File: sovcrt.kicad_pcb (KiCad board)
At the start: 2 copper layers, 51.8 x 41.2 mm, 13 parts, among them J1 Conn_01x02_Male, J2 Conn_01x02_Male, J3 Conn_01x03_Male, U1 LM2575BT-ADJ

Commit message: With @'RueNahcMohr's feedback hack.
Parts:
- added D2: 1N4148, Diode_THT:D_DO-35_SOD27_P7.62mm_Horizontal, F.Cu at (114.8, 84.3)
- added RV1: 5k, Potentiometer_THT:Potentiometer_Bourns_3266P_Horizontal, F.Cu at (119.9, 102.6)
- R1: value 1k -> 4.7k
- R2: value 50 -> 220k; footprint Resistor_THT:R_Axial_DIN0207_L6.3mm_D2.5mm_P10.16mm_Horizontal -> Resistor_THT:R_Axial_DIN0204_L3.6mm_D1.6mm_P7.62mm_Horizontal
- moved R1 7.10 mm to (110.5, 92.1), turned to 90 degrees
- moved J2 6.23 mm to (114.3, 110.2)
- moved TP2 2.11 mm to (122.4, 93.5)
- moved R2 1.17 mm to (117.3, 95.0), turned to 180 degrees
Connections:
- R1 pad 1: Net-(R1-Pad1) -> GND
- R1 pad 2: GND -> Net-(D2-Pad1)
- R2 pad 1: Net-(C2-Pad1) -> Net-(D2-Pad2)
- R2 pad 2: Net-(R1-Pad1) -> +12V
- U1 pad 4: Net-(R1-Pad1) -> Net-(D2-Pad2)
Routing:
- net Net-(D2-Pad1): track 0.00 -> 20.6 mm
- net Net-(D2-Pad2): track 0.00 -> 15.5 mm
- net Net-(R1-Pad1): track 15.3 -> 0.00 mm
- net +12V: track 31.1 -> 43.9 mm
- net Net-(C2-Pad1): track 39.0 -> 47.4 mm
- net Net-(J2-Pad1): track 36.6 -> 29.8 mm
- net GND: track 56.9 -> 53.1 mm
- net Net-(J2-Pad2): track 10.7 -> 14.0 mm
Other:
- board text added: "8LK3B"
- board text added: "8LK3B CRT BASE Copyright (C) toby@telegraphics.com.au With help from @RueNahcMohr"
- board text added: "Adjust filament voltage Nom 1.36V Max 1.5V Or undervolt to 1.1-1.2V"
- board text added: "Heatsink not reqd"
- board text removed: "8LK3B BASE"

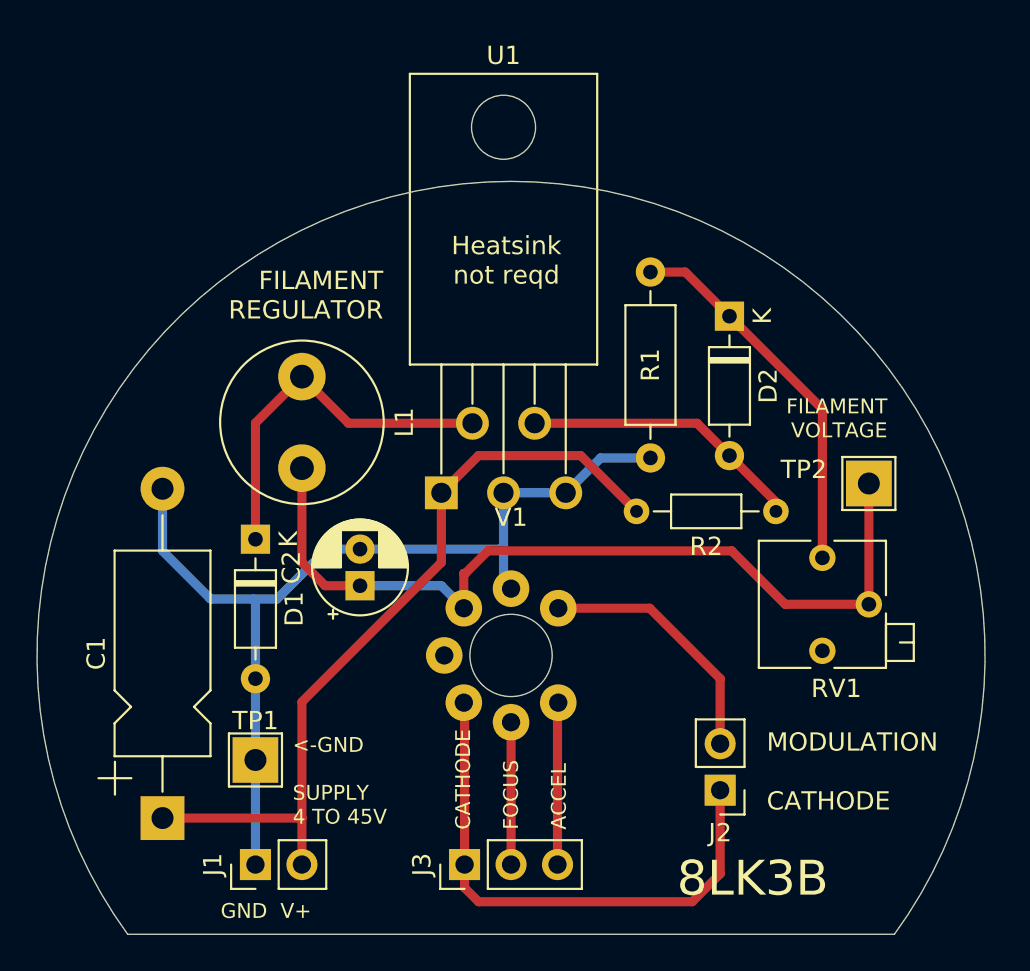
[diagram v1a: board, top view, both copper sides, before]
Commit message: Increase size of output capacitor for proper smoothing; increase diode anode resistor.
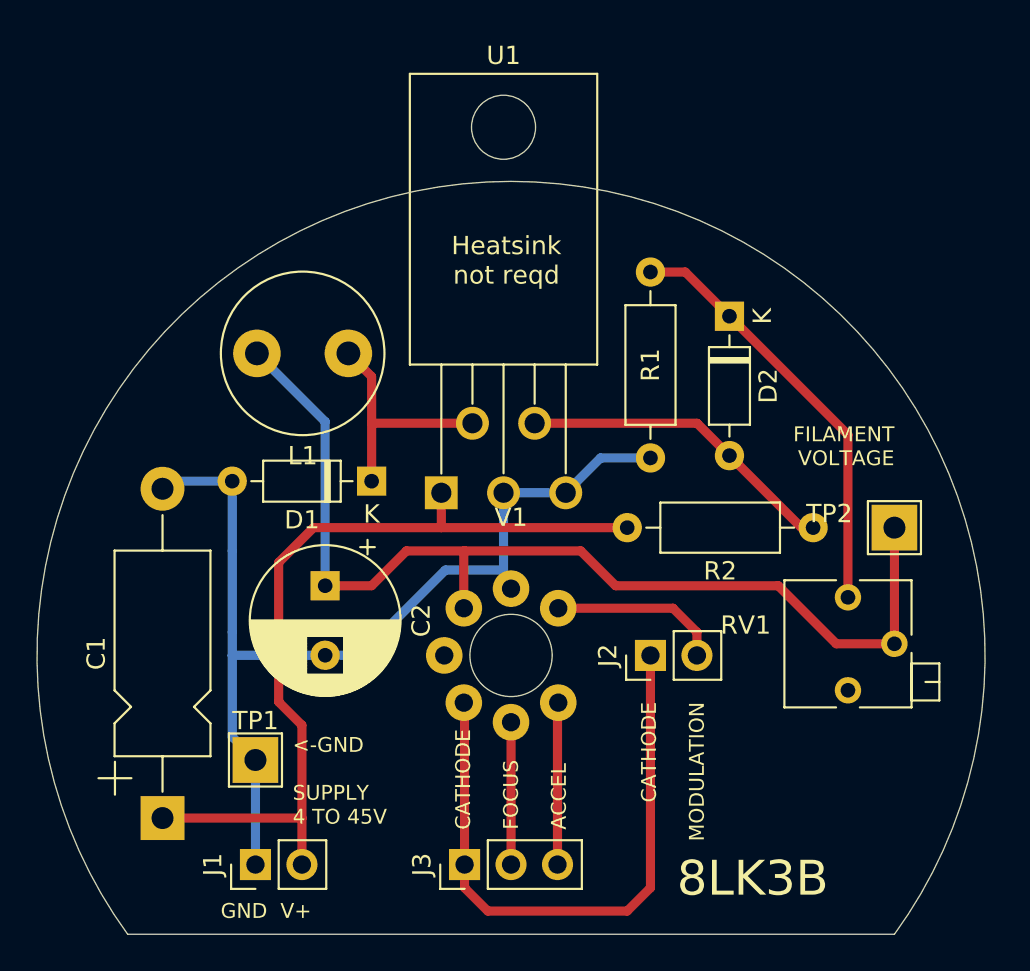
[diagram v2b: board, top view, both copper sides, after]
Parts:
- C2: value 22u 10V -> 470u 16V; footprint Capacitor_THT:CP_Radial_D5.0mm_P2.00mm -> Capacitor_THT:CP_Radial_D8.0mm_P3.80mm
- R2: value 220k -> 1meg; footprint Resistor_THT:R_Axial_DIN0204_L3.6mm_D1.6mm_P7.62mm_Horizontal -> Resistor_THT:R_Axial_DIN0207_L6.3mm_D2.5mm_P10.16mm_Horizontal
- moved J2 8.29 mm to (110.5, 102.9), turned to 90 degrees
- moved D1 7.10 mm to (95.2, 93.3), turned to 180 degrees
- moved L1 2.84 mm to (94.0, 86.4), turned to 180 degrees
- moved TP2 2.79 mm to (123.8, 95.9)
- moved RV1 2.57 mm to (121.3, 104.8)
- moved R2 2.22 mm to (119.4, 95.9)
- moved C2 1.91 mm to (92.7, 99.1), turned to 270 degrees
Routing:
- net Net-(C2-Pad1): track 47.4 -> 57.8 mm
- net Net-(D1-Pad1): track 20.3 -> 13.0 mm
- net Net-(J2-Pad2): track 14.0 -> 9.39 mm
- net Net-(J2-Pad1): track 29.8 -> 34.2 mm
- net GND: track 53.1 -> 56.5 mm
- net Net-(D2-Pad1): track 20.6 -> 23.4 mm
- net +12V: track 43.9 -> 46.4 mm
- net Net-(D2-Pad2): track 15.5 -> 17.6 mm
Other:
- board text added: "CATHODE MODULATION"
- board text removed: "FILAMENT REGULATOR"
- board text removed: "MODULATION CATHODE"

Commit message: Fix capacitor values to fix stability.
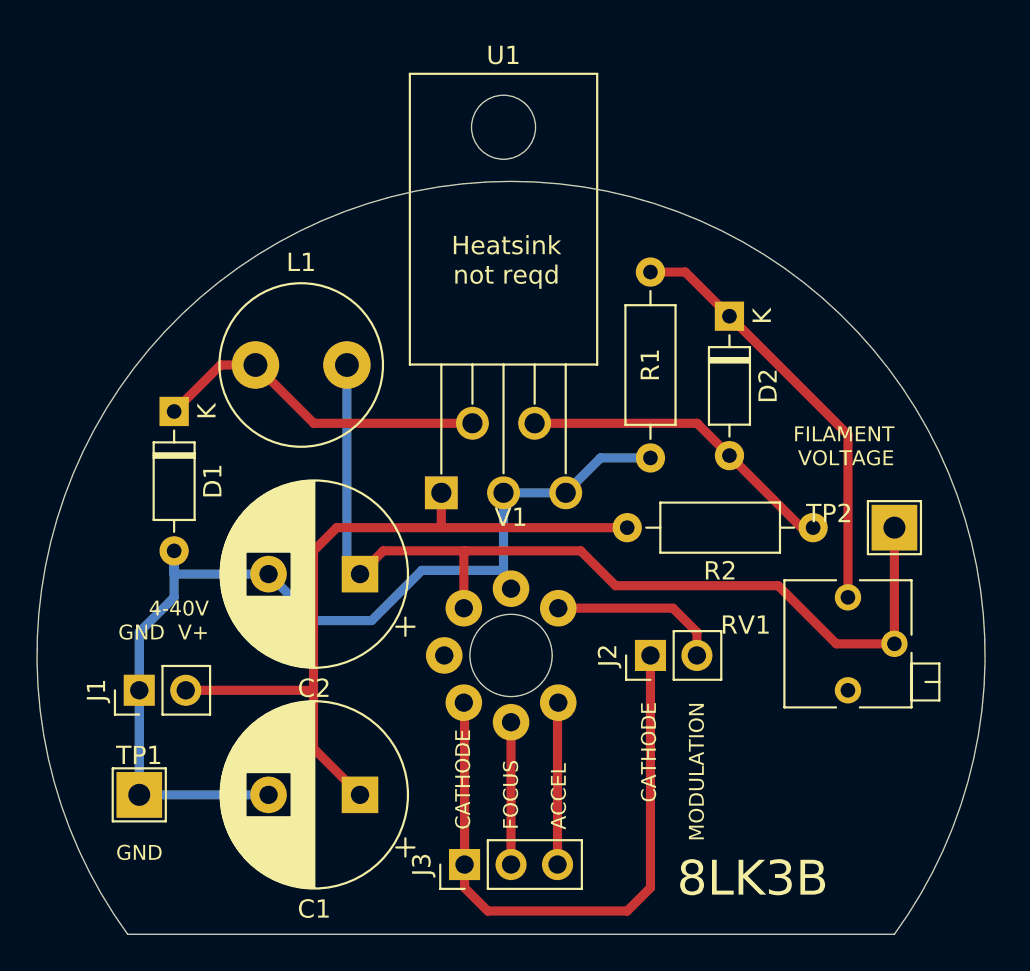
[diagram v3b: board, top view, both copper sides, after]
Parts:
- C1: value 10u 50V -> 220u 50V; footprint Capacitor_THT:CP_Axial_L11.0mm_D5.0mm_P18.00mm_Horizontal -> Capacitor_THT:CP_Radial_D10.0mm_P5.00mm
- C2: value 470u 16V -> 1000u 10V; footprint Capacitor_THT:CP_Radial_D8.0mm_P3.80mm -> Capacitor_THT:CP_Radial_D10.0mm_P5.00mm
- moved D1 11.4 mm to (84.5, 89.5), turned to 270 degrees
- moved J1 11.4 mm to (82.5, 104.8)
- moved C1 10.9 mm to (94.6, 110.5), turned to 180 degrees
- moved TP1 6.63 mm to (82.5, 110.5)
- moved L1 5.12 mm to (88.9, 87.0), turned to 0 degrees
- moved C2 2.01 mm to (94.6, 98.4), turned to 180 degrees
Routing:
- net Net-(D1-Pad1): track 13.0 -> 18.7 mm
- net +12V: track 46.4 -> 40.9 mm
- net Net-(C2-Pad1): track 57.8 -> 53.1 mm
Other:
- board text added: "4-40V GND V+"
- board text added: "8LK3B CRT BASE & FILAMENT REG Copyright (C) 2021 toby@telegraphics.com.au With help from @RueNahcMohr"
- board text added: "GND"
- board text removed: "8LK3B CRT BASE Copyright (C) toby@telegraphics.com.au With help from @RueNahcMohr"
- board text removed: "<-GND SUPPLY 4 TO 45V"
- board text removed: "GND V+"

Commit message: Remove diode hack in favour of a series resistor.
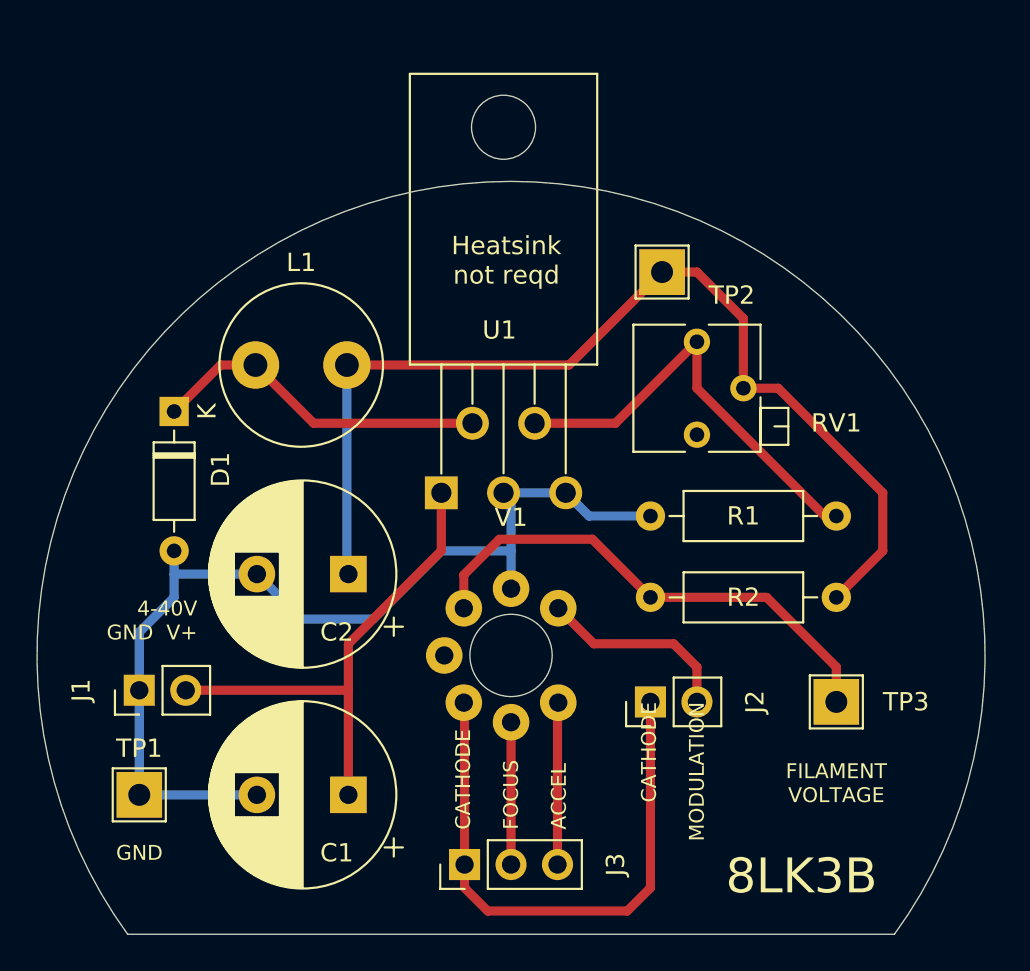
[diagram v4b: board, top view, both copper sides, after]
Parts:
- removed D2: 1N4148, Diode_THT:D_DO-35_SOD27_P7.62mm_Horizontal
- added TP3: TestPoint, TestPoint:TestPoint_THTPad_2.5x2.5mm_Drill1.2mm, F.Cu at (120.7, 105.4)
- R2: value 1meg -> 3R3 1/2W
- moved TP2 18.9 mm to (111.1, 81.9)
- moved RV1 16.2 mm to (113.0, 90.8)
- moved R2 9.67 mm to (110.5, 99.7), turned to 0 degrees
- moved R1 3.17 mm to (110.5, 95.2), turned to 0 degrees
- moved J2 2.54 mm to (110.5, 105.4)
- moved C1 0.63 mm to (94.0, 110.5)
- moved C2 0.63 mm to (94.0, 98.4)
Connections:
- R1 pad 2: Net-(D2-Pad1) -> Net-(R1-Pad2)
- R2 pad 1: Net-(D2-Pad2) -> Net-(R2-Pad1)
- R2 pad 2: +12V -> Net-(C2-Pad1)
- RV1 pad 3: Net-(D2-Pad1) -> Net-(R1-Pad2)
- U1 pad 4: Net-(D2-Pad2) -> Net-(R1-Pad2)
- V1 pad 5: Net-(C2-Pad1) -> Net-(R2-Pad1)
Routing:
- net Net-(R2-Pad1): track 0.00 -> 27.8 mm
- net Net-(R1-Pad2): track 0.00 -> 23.8 mm
- net Net-(D2-Pad1): track 23.4 -> 0.00 mm
- net Net-(D2-Pad2): track 17.6 -> 0.00 mm
- net +12V: track 40.9 -> 27.5 mm
- net Net-(C2-Pad1): track 53.1 -> 57.1 mm
- net Net-(J2-Pad1): track 34.2 -> 31.7 mm
- net Net-(J2-Pad2): track 9.39 -> 10.8 mm
- net GND: track 56.9 -> 55.5 mm
